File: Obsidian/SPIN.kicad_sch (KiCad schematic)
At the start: 1 part, among them U29 OwnTech_SPIN

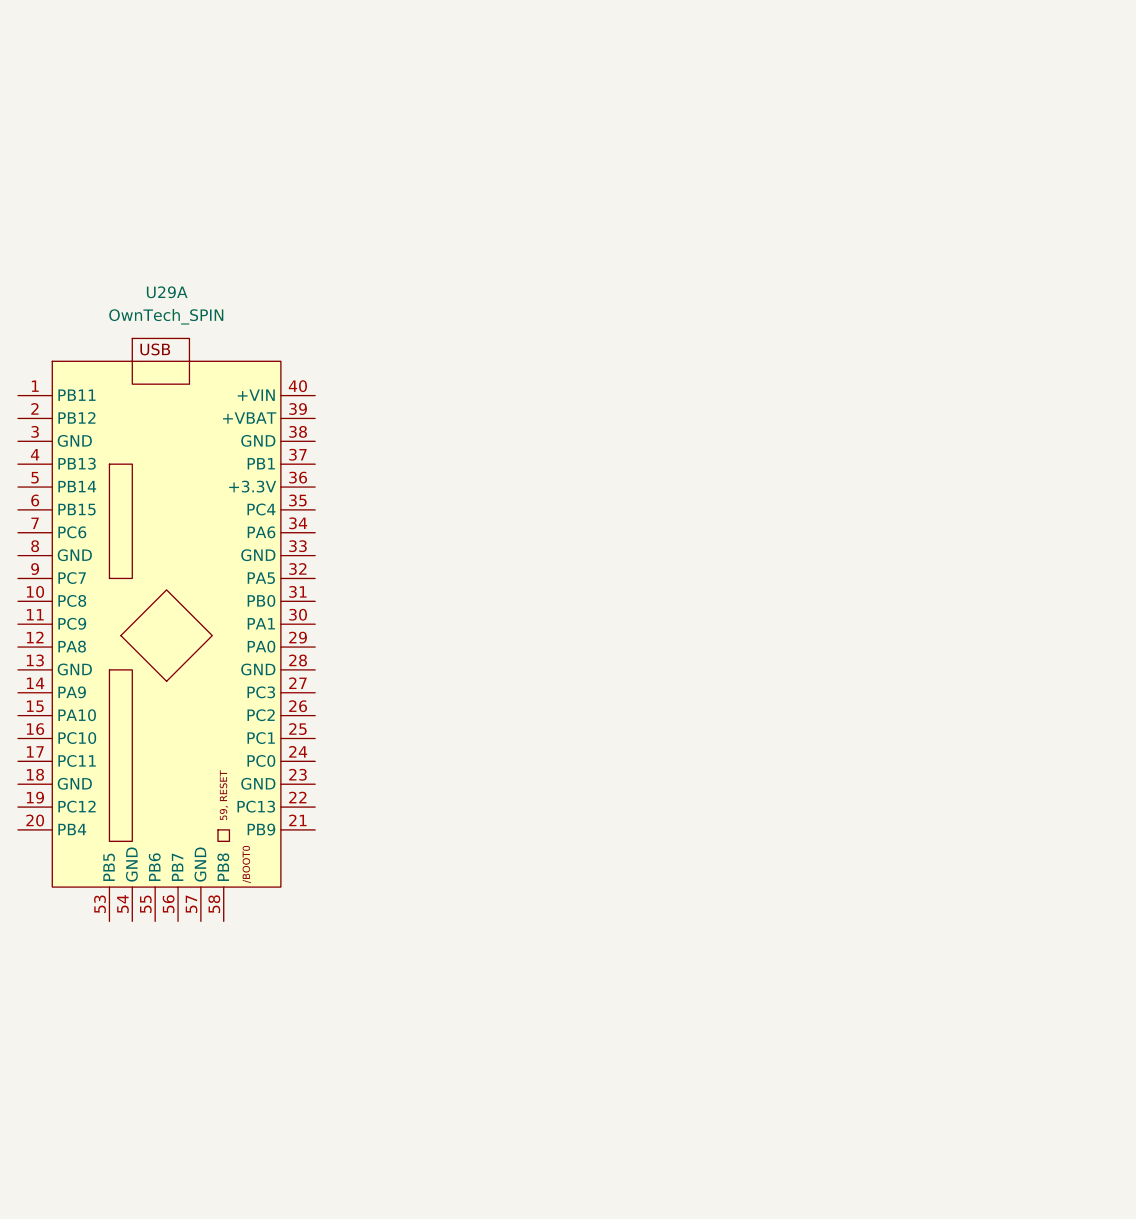
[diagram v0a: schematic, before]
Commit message: adding SPIN, and 5V power for the MCU
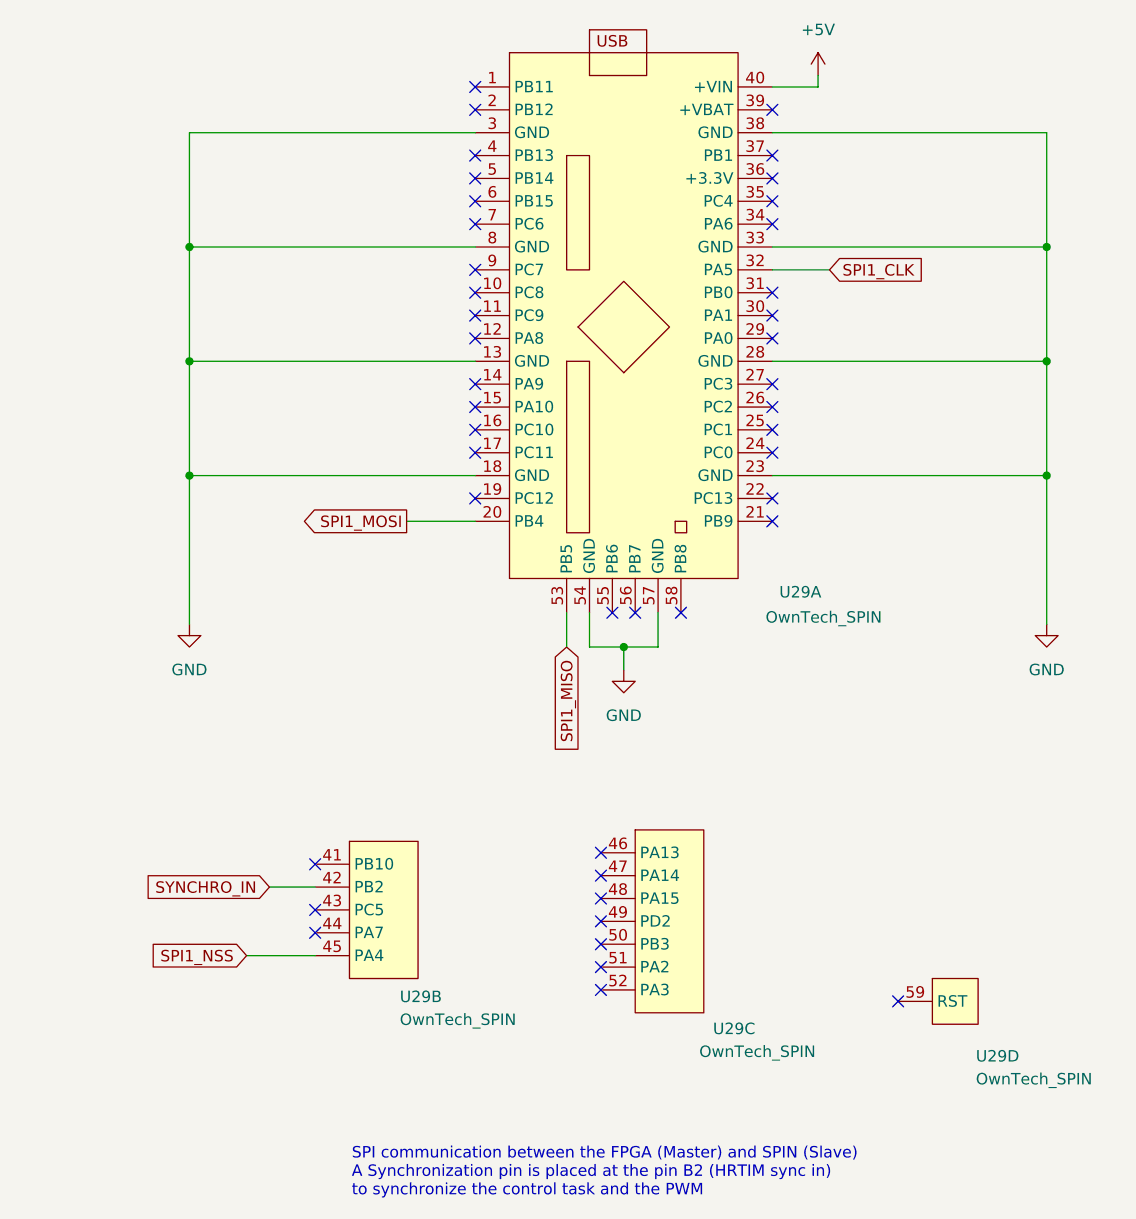
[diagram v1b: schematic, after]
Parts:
- added unit 3 of U29
- added unit 4 of U29
- added unit 2 of U29
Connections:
- net GND: now reaches U29.13 (GND)
- net GND: now also U29.18 (GND), U29.23 (GND), U29.28 (GND), U29.3 (GND), U29.33 (GND), U29.38 (GND), U29.54 (GND), U29.57 (GND), U29.8 (GND)
- net SPI1_MOSI: now reaches U29.20 (PB4)
- net SPI1_CLK: now reaches U29.32 (PA5)
- net +5V: now reaches U29.40 (+VIN)
- net SPI1_MISO: now reaches U29.53 (PB5)
- new net SPI1_NSS: U29.45 (PA4)
- new net SYNCHRO_IN: U29.42 (PB2)
- no-connect marks 0 -> 43
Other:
- note added: "SPI communication between the FPGA (Master) and SPIN (Slave) A Synchronization pin is placed at the pin B2 (HRTIM sync in) to synchronize the control task and the PWM"
